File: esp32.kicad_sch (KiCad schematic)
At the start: 12 parts, among them J2 Conn_01x05_Pin, Q3 MMBT3904, Q4 MMBT3904, Y1 ECS-2520MV-xxx-xx

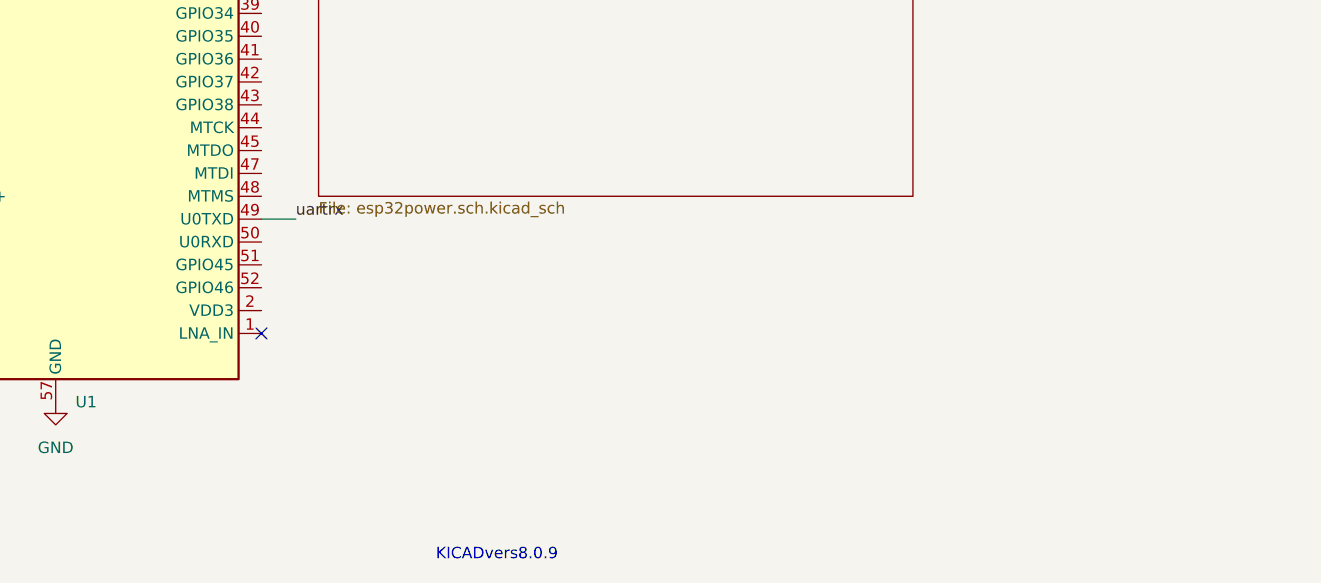
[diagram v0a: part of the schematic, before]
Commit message: addedstm32F413
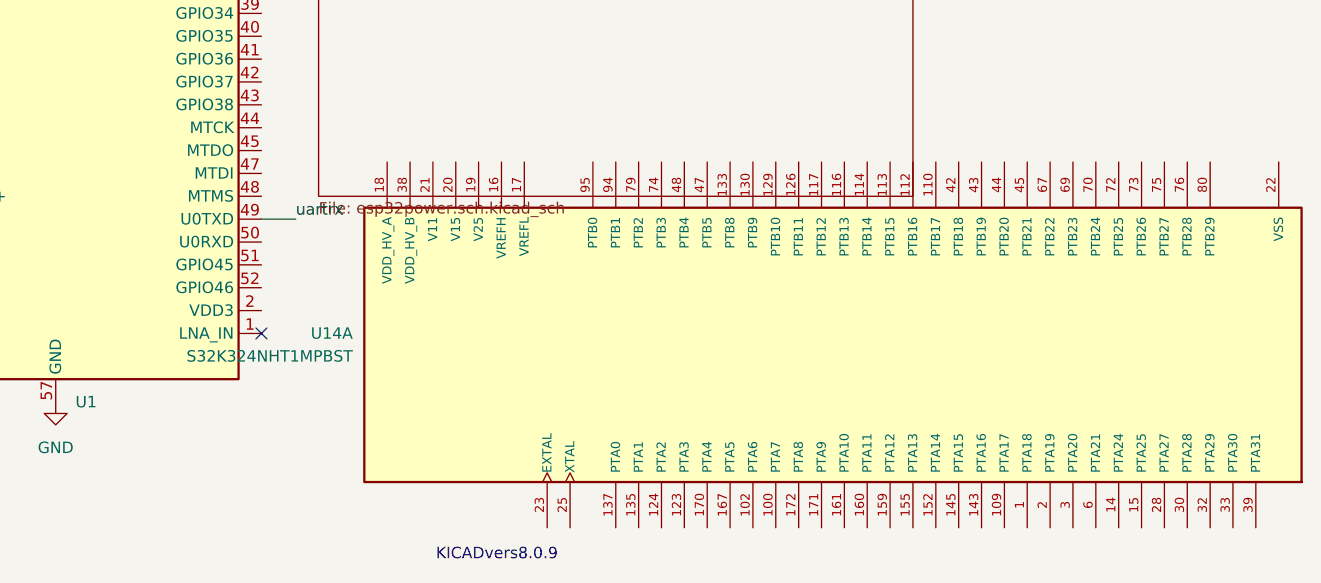
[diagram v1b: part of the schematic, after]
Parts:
- added U14: S32K324NHT1MPBST, commonfootprint:IC_S32K324NHT1MPBST, symbol common:S32K324NHT1MPBST
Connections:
- net at U1.2 (VDD3P3): now also U1.3 (VDD3P3)
- new net V11: U14.106 (V11), U14.149 (V11), U14.21 (V11), U14.59 (V11)
- new net V15: U14.105 (V15), U14.148 (V15), U14.20 (V15), U14.60 (V15)
- new net VDD_HV_A: U14.108 (VDD_HV_A), U14.128 (VDD_HV_A), U14.151 (VDD_HV_A), U14.169 (VDD_HV_A), U14.18 (VDD_HV_A)
- new net VDD_HV_B: U14.38 (VDD_HV_B), U14.57 (VDD_HV_B), U14.77 (VDD_HV_B)
- new net VSS: U14.107 (VSS), U14.127 (VSS), U14.150 (VSS), U14.168 (VSS), U14.22 (VSS), U14.24 (VSS), U14.37 (VSS), U14.58 (VSS), U14.78 (VSS)

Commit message: recloned first commit
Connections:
- net at U1.2 (VDD3P3): now also U1.3 (VDD3P3)
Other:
- moved on the sheet: U14A
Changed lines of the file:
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@@
 	(symbol
 		(lib_id "common:S32K324NHT1MPBST")
-		(at 226.06 148.59 90)
+		(at 222.25 85.09 90)
 		(unit 1)
 		(exclude_from_sim no)
@@
 		(fields_autoplaced yes)
 		(property "Reference" "U14"
-			(at 171.45 147.3199 90)
+			(at 167.64 83.8199 90)
 			(effects
 				(font
@@
 		)
 		(property "Value" "S32K324NHT1MPBST"
-			(at 171.45 149.8599 90)
+			(at 167.64 86.3599 90)
 			(effects
 				(font
@@
 		)
 		(property "Footprint" "commonfootprint:IC_S32K324NHT1MPBST"
-			(at 226.06 148.59 0)
+			(at 222.25 85.09 0)
 			(effects
 				(font
@@
 		)
 		(property "Datasheet" ""
-			(at 226.06 148.59 0)
+			(at 222.25 85.09 0)
 			(effects
 				(font
@@
 		)
 		(property "Description" ""
-			(at 226.06 148.59 0)
+			(at 222.25 85.09 0)
 			(effects
 				(font
@@
 		)
 		(property "MF" "NXP Semiconductors"
-			(at 226.06 148.59 0)
+			(at 222.25 85.09 0)
 			(effects
 				(font
@@
 		)
 		(property "MAXIMUM_PACKAGE_HEIGHT" "1.65 mm"
-			(at 226.06 148.59 0)
+			(at 222.25 85.09 0)
 			(effects
 				(font
@@
 		)
 		(property "Package" "QFP-172 NXP"
-			(at 226.06 148.59 0)
+			(at 222.25 85.09 0)
 			(effects
 				(font
@@
 		)
 		(property "Price" "None"
-			(at 226.06 148.59 0)
+			(at 222.25 85.09 0)
 			(effects
 				(font
@@
 		)
 		(property "Check_prices" "https://www.snapeda.com/parts/S32K324NHT1MPBST/NXP+Semiconductors/view-part/?ref=eda"
-			(at 226.06 148.59 0)
+			(at 222.25 85.09 0)
 			(effects
 				(font
@@
 		)
 		(property "STANDARD" "Manufacturer Recommendations"
-			(at 226.06 148.59 0)
+			(at 222.25 85.09 0)
 			(effects
 				(font
@@
 		)
 		(property "PARTREV" "7"
-			(at 226.06 148.59 0)
+			(at 222.25 85.09 0)
 			(effects
 				(font
@@
 		)
 		(property "SnapEDA_Link" "https://www.snapeda.com/parts/S32K324NHT1MPBST/NXP+Semiconductors/view-part/?ref=snap"
-			(at 226.06 148.59 0)
+			(at 222.25 85.09 0)
 			(effects
 				(font
@@
 		)
 		(property "MP" "S32K324NHT1MPBST"
-			(at 226.06 148.59 0)
+			(at 222.25 85.09 0)
 			(effects
 				(font
@@
 		)
 		(property "Description_1" "\n                        \n                            ARM® Cortex®-M7 Automotive, AEC-Q100, S32K3 Microcontroller IC 32-Bit Dual-Core 160MHz 4MB (4M x 8) FLASH 172-QFP (16x16)\n                        \n"
-			(at 226.06 148.59 0)
+			(at 222.25 85.09 0)
 			(effects
 				(font
@@
 		)
 		(property "SNAPEDA_PN" "121580"
-			(at 226.06 148.59 0)
+			(at 222.25 85.09 0)
 			(effects
 				(font
@@
 		)
 		(property "Availability" "In Stock"
-			(at 226.06 148.59 0)
+			(at 222.25 85.09 0)
 			(effects
 				(font
@@
 		)
 		(property "MANUFACTURER" "NXP Semiconductors"
-			(at 226.06 148.59 0)
+			(at 222.25 85.09 0)
 			(effects
 				(font

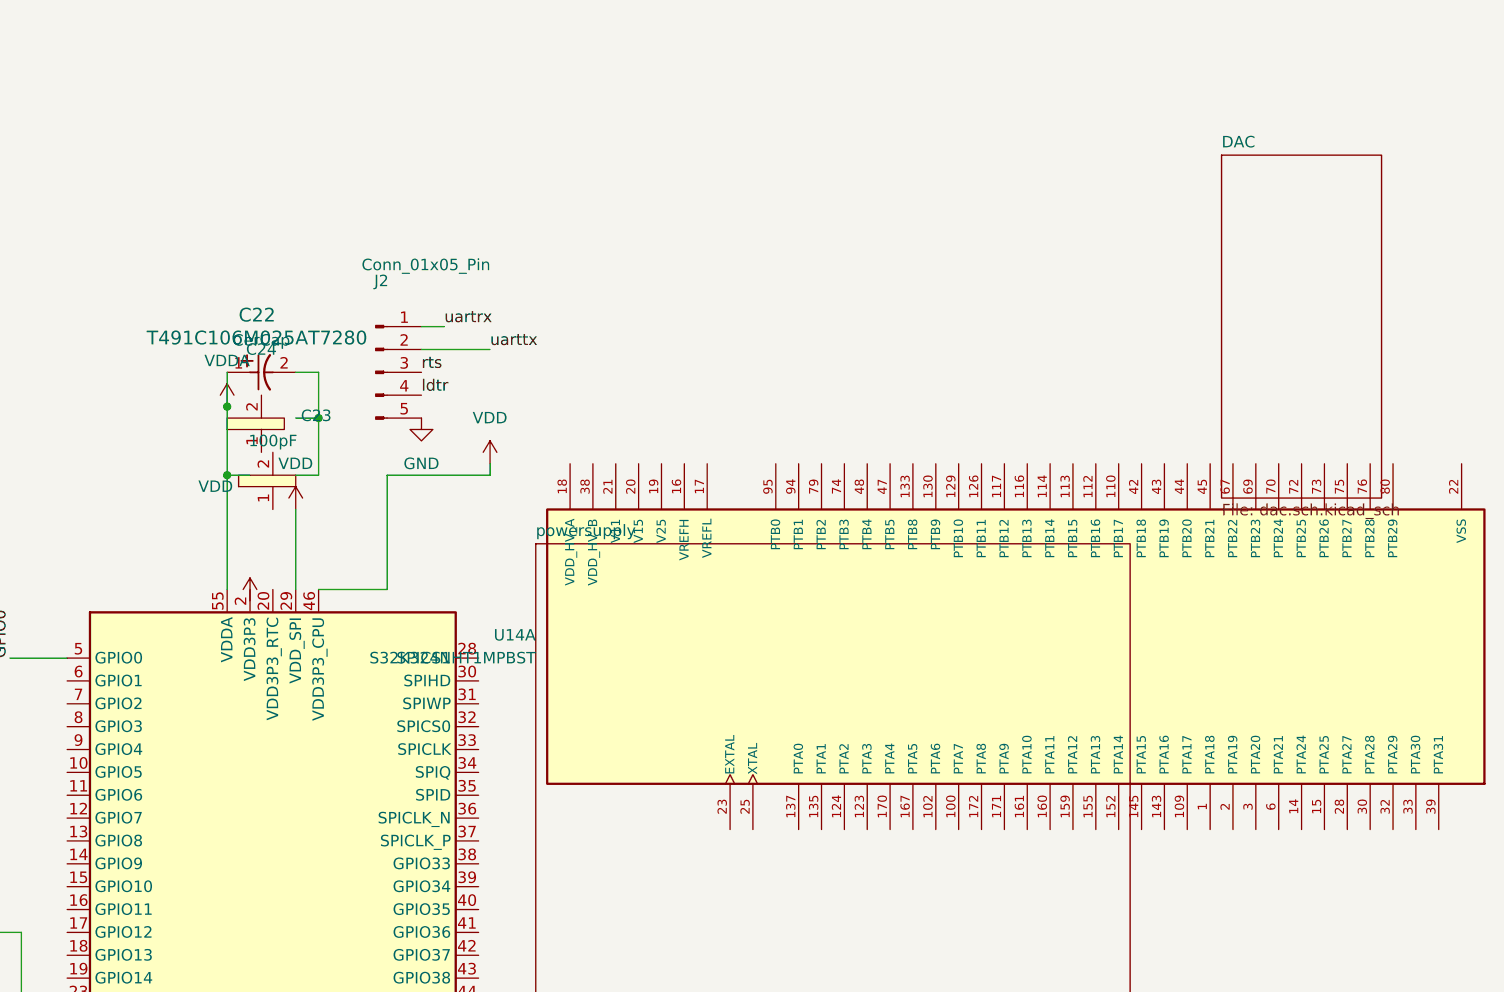
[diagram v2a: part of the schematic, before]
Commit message: added psucomponets to esp32 IC
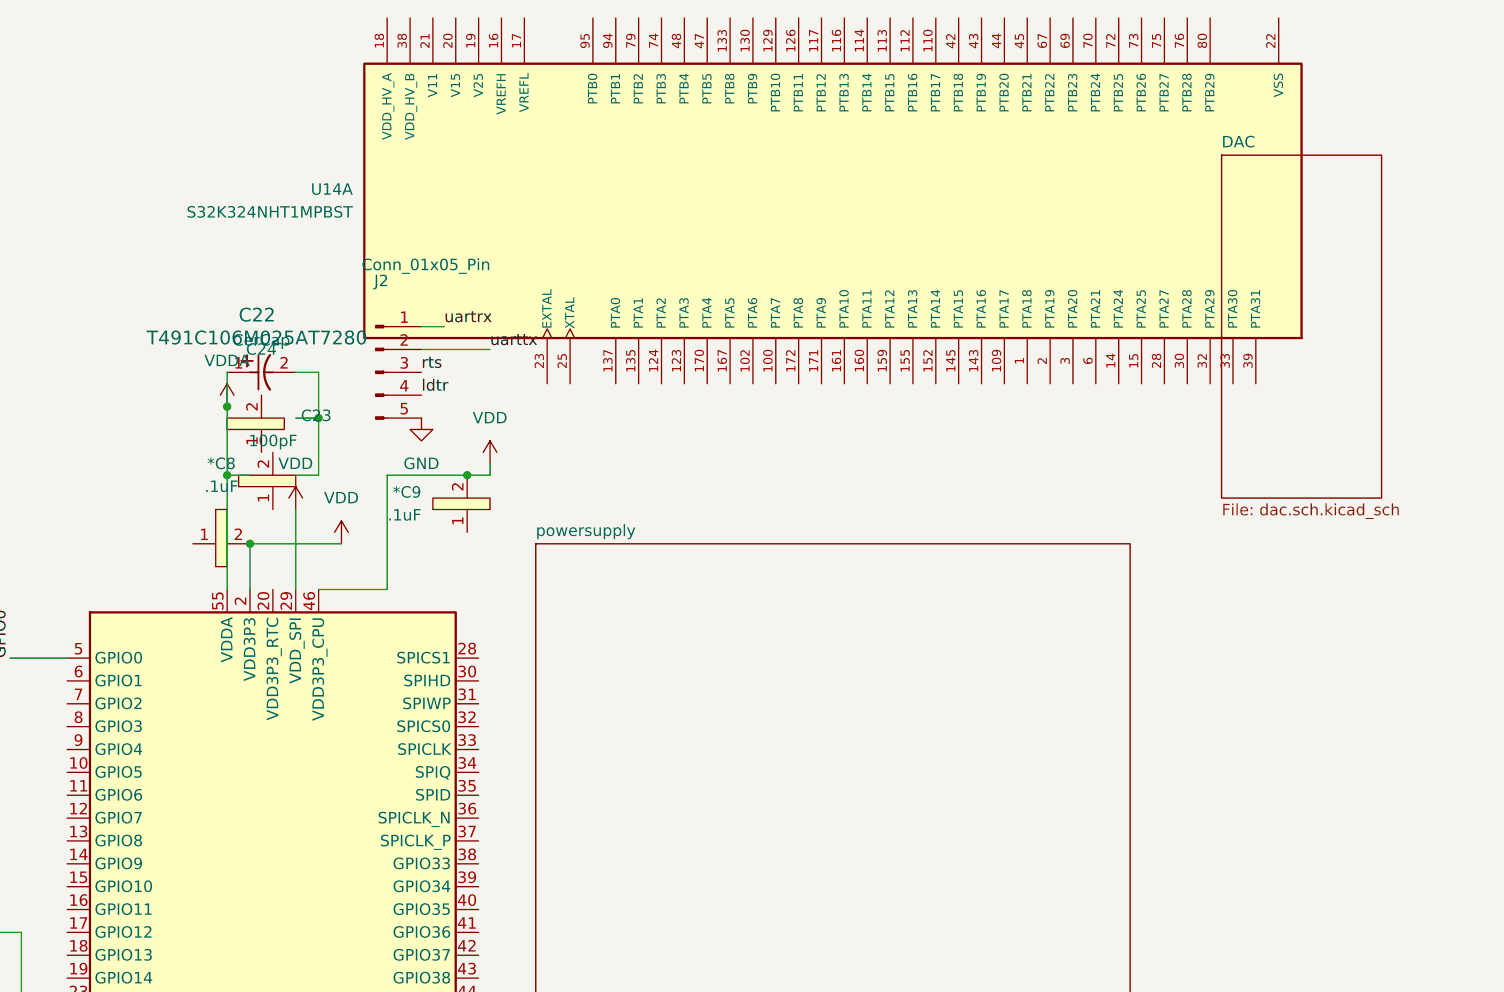
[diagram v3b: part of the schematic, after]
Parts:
- added *C8, *C9: .1uF, commonfootprint:Ceramic0603, symbol common:CerCap
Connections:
- net VDD: now also U1.2 (VDD3P3), U1.3 (VDD3P3), *C8.2, *C9.2
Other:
- moved on the sheet: U14A
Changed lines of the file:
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@@
+	)
+	(junction
+		(at 135.89 73.66)
+		(diameter 0)
+		(color 0 0 0 0)
 	)
 	(junction
@@
 	)
 	(junction
+		(at 160.02 66.04)
+		(diameter 0)
+		(color 0 0 0 0)
+	)
+	(junction
 		(at 66.04 30.48)
 		(diameter 0)
@@
 	(wire
 		(pts
+			(xy 135.89 73.66) (xy 135.89 78.74)
+		)
+		(stroke
+			(width 0)
+			(type default)
+		)
+	)
+	(wire
+		(pts
 			(xy 67.31 132.08) (xy 69.85 132.08)
 		)
@@
 	(wire
 		(pts
+			(xy 146.05 73.66) (xy 135.89 73.66)
+		)
+		(stroke
+			(width 0)
+			(type default)
+		)
+	)
+	(wire
+		(pts
 			(xy 90.17 132.08) (xy 104.14 132.08)
 		)
@@
 	(wire
 		(pts
-			(xy 151.13 66.04) (xy 162.56 66.04)
+			(xy 151.13 66.04) (xy 160.02 66.04)
 		)
 		(stroke
@@
 		(pts
 			(xy 115.57 142.24) (xy 115.57 139.7)
+		)
+		(stroke
+			(width 0)
+			(type default)
+		)
+	)
+	(wire
+		(pts
+			(xy 160.02 66.04) (xy 162.56 66.04)
 		)
 		(stroke
@@
 	(symbol
 		(lib_id "common:CerCap")
+		(at 133.35 73.66 0)
+		(unit 1)
+		(exclude_from_sim no)
+		(in_bom yes)
+		(on_board yes)
+		(dnp no)
+		(fields_autoplaced yes)
+		(property "Reference" "*C8"
+			(at 132.715 64.77 0)
+			(effects
+				(font
+					(size 1.27 1.27)
+				)
+			)
+		)
+		(property "Value" ".1uF"
+			(at 132.715 67.31 0)
+			(effects
+				(font
+					(size 1.27 1.27)
+				)
+			)
+		)
+		(property "Footprint" "commonfootprint:Ceramic0603"
+			(at 133.35 66.802 0)
+			(effects
+				(font
+					(size 1.27 1.27)
+				)
+				(hide yes)
+			)
+		)
+		(property "Datasheet" ""
+			(at 133.35 73.66 0)
+			(effects
+				(font
+					(size 1.27 1.27)
+				)
+				(hide yes)
+			)
+		)
+		(property "Description" ""
+			(at 133.35 73.66 0)
+			(effects
+				(font
+					(size 1.27 1.27)
+				)
+				(hide yes)
+			)
+		)
+		(pin "2"
+		)
+		(pin "1"
+		)
+		(instances
+			(project ""
+				(path "/c4754426-a41b-4341-9d09-2e389619f3d6"
+					(reference "*C8")
+					(unit 1)
+				)
+			)
+		)
+	)
+	(symbol
+		(lib_id "common:CerCap")
 		(at 138.43 66.04 90)
 		(unit 1)
@@
 				(path "/c4754426-a41b-4341-9d09-2e389619f3d6"
 					(reference "C23")
+					(unit 1)
+				)
+			)
+		)
+	)
+	(symbol
+		(lib_id "power:VDD")
+		(at 146.05 73.66 0)
+		(unit 1)
+		(exclude_from_sim no)
+		(in_bom yes)
+		(on_board yes)
+		(dnp no)
+		(fields_autoplaced yes)
+		(property "Reference" "#PWR15"
+			(at 146.05 77.47 0)
+			(effects
+				(font
+					(size 1.27 1.27)
+				)
+				(hide yes)
+			)
+		)
+		(property "Value" "VDD"
+			(at 146.05 68.58 0)
+			(effects
+				(font
+					(size 1.27 1.27)
+				)
+			)
+		)
+		(property "Footprint" ""
+			(at 146.05 73.66 0)
+			(effects
+				(font
+					(size 1.27 1.27)
+				)
+				(hide yes)
+			)
+		)
+		(property "Datasheet" ""
+			(at 146.05 73.66 0)
+			(effects
+				(font
+					(size 1.27 1.27)
+				)
+				(hide yes)
+			)
+		)
+		(property "Description" "Power symbol creates a global label with name \"VDD\""
+			(at 146.05 73.66 0)
+			(effects
+				(font
+					(size 1.27 1.27)
+				)
+				(hide yes)
+			)
+		)
+		(pin "1"
+		)
+		(instances
+			(project "esp32"
+				(path "/c4754426-a41b-4341-9d09-2e389619f3d6"
+					(reference "#PWR15")
 					(unit 1)
 				)
@@
 	(symbol
 		(lib_id "common:S32K324NHT1MPBST")
-		(at 222.25 85.09 90)
+		(at 201.93 35.56 90)
 		(unit 1)
 		(exclude_from_sim no)
@@
 		(fields_autoplaced yes)
 		(property "Reference" "U14"
-			(at 167.64 83.8199 90)
+			(at 147.32 34.2899 90)
 			(effects
 				(font
@@
 		)
 		(property "Value" "S32K324NHT1MPBST"
-			(at 167.64 86.3599 90)
+			(at 147.32 36.8299 90)
 			(effects
 				(font
@@
 		)
 		(property "Footprint" "commonfootprint:IC_S32K324NHT1MPBST"
-			(at 222.25 85.09 0)
+			(at 201.93 35.56 0)
 			(effects
 				(font
@@
 		)
 		(property "Datasheet" ""
-			(at 222.25 85.09 0)
+			(at 201.93 35.56 0)
 			(effects
 				(font
@@
 		)
 		(property "Description" ""
-			(at 222.25 85.09 0)
+			(at 201.93 35.56 0)
 			(effects
 				(font
@@
 		)
 		(property "MF" "NXP Semiconductors"
-			(at 222.25 85.09 0)
+			(at 201.93 35.56 0)
 			(effects
 				(font
@@
 		)
 		(property "MAXIMUM_PACKAGE_HEIGHT" "1.65 mm"
-			(at 222.25 85.09 0)
+			(at 201.93 35.56 0)
 			(effects
 				(font
@@
 		)
 		(property "Package" "QFP-172 NXP"
-			(at 222.25 85.09 0)
+			(at 201.93 35.56 0)
 			(effects
 				(font
@@
 		)
 		(property "Price" "None"
-			(at 222.25 85.09 0)
+			(at 201.93 35.56 0)
 			(effects
 				(font
@@
 		)
 		(property "Check_prices" "https://www.snapeda.com/parts/S32K324NHT1MPBST/NXP+Semiconductors/view-part/?ref=eda"
-			(at 222.25 85.09 0)
+			(at 201.93 35.56 0)
 			(effects
 				(font
@@
 		)
 		(property "STANDARD" "Manufacturer Recommendations"
-			(at 222.25 85.09 0)
+			(at 201.93 35.56 0)
 			(effects
 				(font
@@
 		)
 		(property "PARTREV" "7"
-			(at 222.25 85.09 0)
+			(at 201.93 35.56 0)
 			(effects
 				(font
@@
 		)
 		(property "SnapEDA_Link" "https://www.snapeda.com/parts/S32K324NHT1MPBST/NXP+Semiconductors/view-part/?ref=snap"
-			(at 222.25 85.09 0)
+			(at 201.93 35.56 0)
 			(effects
 				(font
@@
 		)
 		(property "MP" "S32K324NHT1MPBST"
-			(at 222.25 85.09 0)
+			(at 201.93 35.56 0)
 			(effects
 				(font
@@
 		)
 		(property "Description_1" "\n                        \n                            ARM® Cortex®-M7 Automotive, AEC-Q100, S32K3 Microcontroller IC 32-Bit Dual-Core 160MHz 4MB (4M x 8) FLASH 172-QFP (16x16)\n                        \n"
-			(at 222.25 85.09 0)
+			(at 201.93 35.56 0)
 			(effects
 				(font
@@
 		)
 		(property "SNAPEDA_PN" "121580"
-			(at 222.25 85.09 0)
+			(at 201.93 35.56 0)
 			(effects
 				(font
@@
 		)
 		(property "Availability" "In Stock"
-			(at 222.25 85.09 0)
+			(at 201.93 35.56 0)
 			(effects
 				(font
@@
 		)
 		(property "MANUFACTURER" "NXP Semiconductors"
-			(at 222.25 85.09 0)
+			(at 201.93 35.56 0)
 			(effects
 				(font
@@
 	)
 	(symbol
-		(lib_id "power:VDD")
-		(at 135.89 80.01 0)
-		(unit 1)
-		(exclude_from_sim no)
-		(in_bom yes)
-		(on_board yes)
-		(dnp no)
-		(property "Reference" "#PWR15"
-			(at 135.89 83.82 0)
-			(effects
-				(font
-					(size 1.27 1.27)
-				)
-				(hide yes)
-			)
-		)
-		(property "Value" "VDD"
-			(at 132.08 67.31 0)
-			(effects
-				(font
-					(size 1.27 1.27)
-				)
-			)
-		)
-		(property "Footprint" ""
-			(at 135.89 80.01 0)
-			(effects
-				(font
-					(size 1.27 1.27)
-				)
-				(hide yes)
-			)
-		)
-		(property "Datasheet" ""
-			(at 135.89 80.01 0)
-			(effects
-				(font
-					(size 1.27 1.27)
-				)
-				(hide yes)
-			)
-		)
-		(property "Description" "Power symbol creates a global label with name \"VDD\""
-			(at 135.89 80.01 0)
-			(effects
-				(font
-					(size 1.27 1.27)
-				)
-				(hide yes)
-			)
-		)
-		(pin "1"
-		)
-		(instances
-			(project ""
-				(path "/c4754426-a41b-4341-9d09-2e389619f3d6"
-					(reference "#PWR15")
-					(unit 1)
-				)
-			)
-		)
-	)
-	(symbol
 		(lib_id "power:GND")
 		(at 69.85 137.16 0)
@@
 					(unit 1)
 				)
+			)
+		)
+	)
+	(symbol
+		(lib_id "common:CerCap")
+		(at 160.02 68.58 90)
+		(unit 1)
+		(exclude_from_sim no)
+		(in_bom yes)
+		(on_board yes)
+		(dnp no)
+		(fields_autoplaced yes)
+		(property "Reference" "*C9"
+			(at 154.94 67.9449 90)
+			(effects
+				(font
+					(size 1.27 1.27)
+				)
+				(justify left)
+			)
+		)
+		(property "Value" ".1uF"
+			(at 154.94 70.4849 90)
+			(effects
+				(font
+					(size 1.27 1.27)
+				)
+				(justify left)
+			)
+		)
+		(property "Footprint" "commonfootprint:Ceramic0603"
+			(at 153.162 68.58 0)
+			(effects
+				(font
+					(size 1.27 1.27)
+				)
+				(hide yes)
+			)
+		)
+		(property "Datasheet" ""
+			(at 160.02 68.58 0)
+			(effects
+				(font
+					(size 1.27 1.27)
+				)
+				(hide yes)
+			)
+		)
+		(property "Description" ""
+			(at 160.02 68.58 0)
+			(effects
+				(font
+					(size 1.27 1.27)
+				)
+				(hide yes)
+			)
+		)
+		(pin "2"
+		)
+		(pin "1"
+		)
+		(instances
+			(project "esp32"
+				(path "/c4754426-a41b-4341-9d09-2e389619f3d6"
+					(reference "*C9")
+					(unit 1)
+				)
